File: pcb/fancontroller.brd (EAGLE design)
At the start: 42.5 x 63.3 mm, 109 parts, among them CN1 USB-MICROB-2TABS, Q1 AO3401, Q10 AO3401, Q11 AO3402, Q12 AO3402, Q13 AO3402, Q14 AO3402, Q15 AO3402, Q16 AO3402, Q17 AO3402, Q18 AO3402, Q2 AO3401, Q3 AO3401, Q4 AO3401, Q5 AO3401, Q6 AO3401, Q7 AO3401, Q8 AO3401, Q9 8M, U1 RT9193, U2 STM32F103-48LQFP

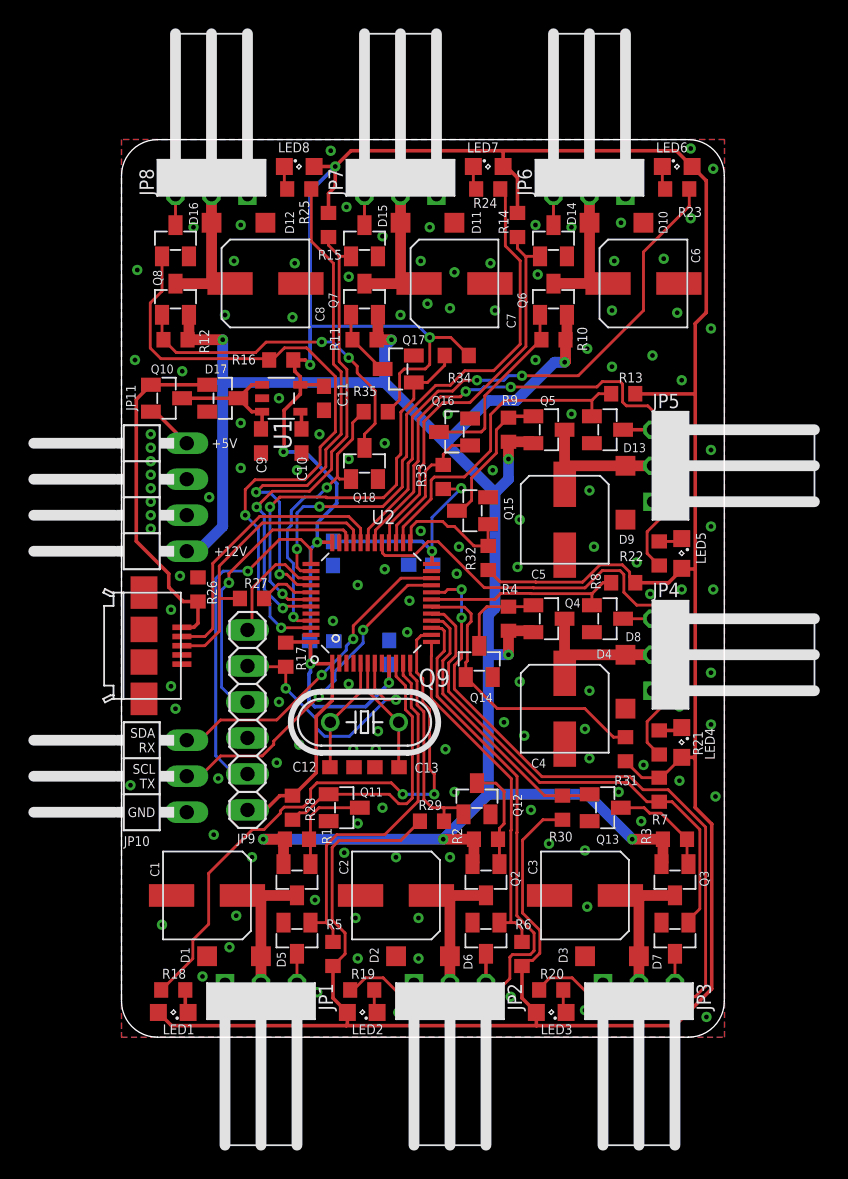
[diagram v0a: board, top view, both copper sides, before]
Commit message: pcb: Move misc designators for better readability
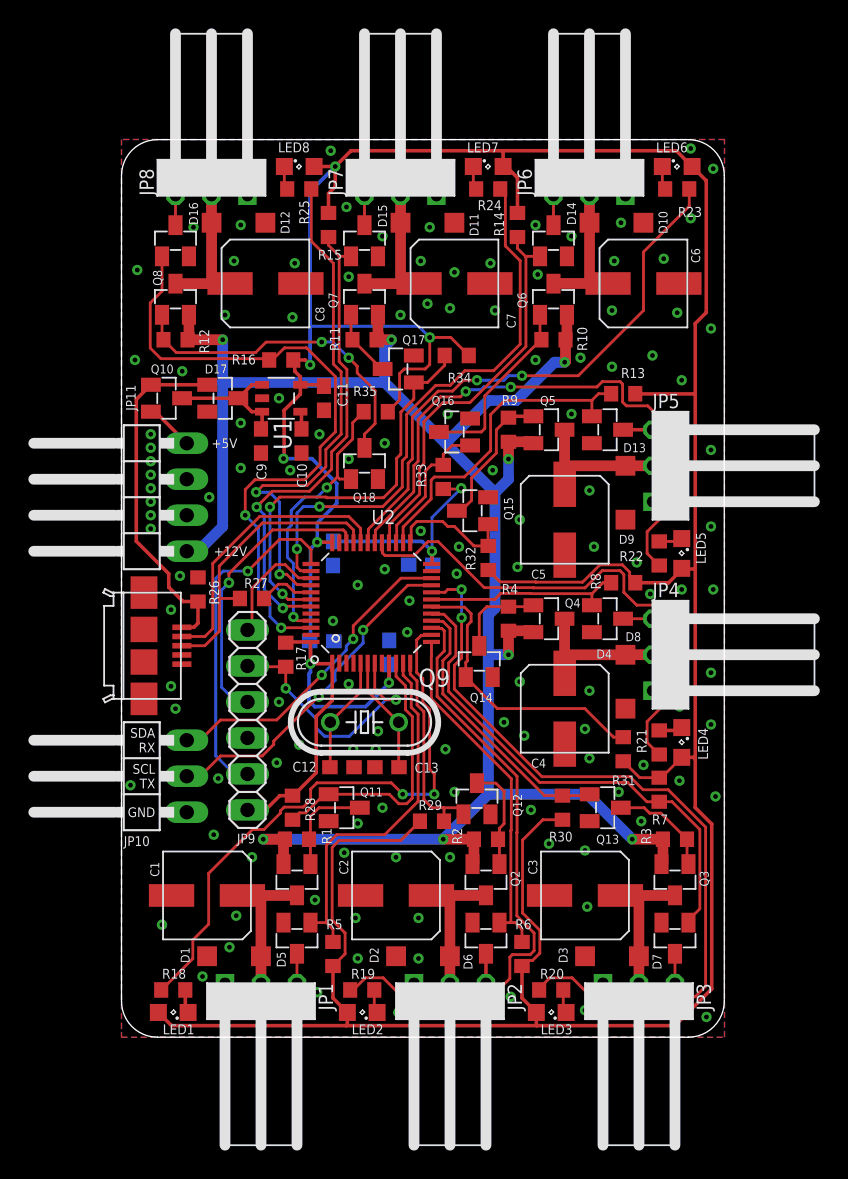
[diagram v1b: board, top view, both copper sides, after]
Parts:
- moved R31 0.16 mm to (35.4, 21.9)
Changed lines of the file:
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@@
 <layer number="46" name="Milling" color="3" fill="1" visible="no" active="yes"/>
 <layer number="47" name="Measures" color="7" fill="1" visible="no" active="yes"/>
-<layer number="48" name="Document" color="7" fill="1" visible="no" active="yes"/>
-<layer number="49" name="Reference" color="7" fill="1" visible="no" active="yes"/>
+<layer number="48" name="Document" color="7" fill="1" visible="yes" active="yes"/>
+<layer number="49" name="Reference" color="7" fill="1" visible="yes" active="yes"/>
 <layer number="50" name="dxf" color="7" fill="1" visible="no" active="no"/>
 <layer number="51" name="tDocu" color="7" fill="1" visible="yes" active="yes"/>
@@
 </element>
 <element name="LED4" library="led" package="SML0805" value="" x="39.52875" y="22.38375" smashed="yes" rot="R270">
-<attribute name="NAME" x="41.16375" y="23.4075" size="0.7" layer="25" rot="R270"/>
+<attribute name="NAME" x="40.6875" y="23.4075" size="0.7" layer="25" rot="R270"/>
 <attribute name="VALUE" x="37.52875" y="23.88375" size="1.27" layer="27" rot="R270"/>
 </element>
@@
 </element>
 <element name="R21" library="tuetuopay" package="R0603" value="330" x="37.94125" y="22.38375" smashed="yes" rot="R90">
-<attribute name="NAME" x="40.3225" y="23.1775" size="0.7" layer="25" rot="R270"/>
+<attribute name="NAME" x="36.35375" y="23.33625" size="0.7" layer="25" rot="R270"/>
 </element>
 <element name="R22" library="tuetuopay" package="R0603" value="330" x="37.94125" y="35.71875" smashed="yes" rot="R90">
@@
 </element>
 <element name="R24" library="tuetuopay" package="R0603" value="330" x="25.87625" y="61.43625" smashed="yes" rot="R180">
-<attribute name="NAME" x="26.51125" y="60.80125" size="0.7" layer="25" rot="R180"/>
+<attribute name="NAME" x="26.82875" y="60.6425" size="0.7" layer="25" rot="R180"/>
 </element>
 <element name="R25" library="tuetuopay" package="R0603" value="330" x="12.54125" y="61.43625" smashed="yes" rot="R180">
@@
 </element>
 <element name="R13" library="tuetuopay" package="R0603" value="10k" x="35.40125" y="46.99" smashed="yes">
-<attribute name="NAME" x="35.08375" y="47.78375" size="0.7" layer="25"/>
+<attribute name="NAME" x="35.2425" y="48.10125" size="0.7" layer="25"/>
 </element>
 <element name="R10" library="tuetuopay" package="R0603" value="100k" x="30.48" y="50.8" smashed="yes">
@@
 </element>
 <element name="R14" library="tuetuopay" package="R0603" value="10k" x="27.94" y="58.89625" smashed="yes" rot="R90">
-<attribute name="NAME" x="27.305" y="58.26125" size="0.7" layer="25" rot="R90"/>
+<attribute name="NAME" x="26.9875" y="58.1025" size="0.7" layer="25" rot="R90"/>
 </element>
 <element name="R11" library="tuetuopay" package="R0603" value="100k" x="17.145" y="50.8" smashed="yes">
@@
 </element>
 <element name="C9" library="tuetuopay" package="0603" value="1u" x="9.8425" y="43.65625" smashed="yes" rot="R270">
-<attribute name="NAME" x="9.525" y="42.545" size="0.7" layer="25" rot="R270"/>
+<attribute name="NAME" x="9.525" y="42.06875" size="0.7" layer="25" rot="R270"/>
 </element>
 <element name="C11" library="tuetuopay" package="0603" value="1u" x="14.2875" y="46.6725" smashed="yes" rot="R270">
@@
 </element>
 <element name="C10" library="tuetuopay" package="0603" value="22n" x="12.7" y="43.65625" smashed="yes" rot="R270">
-<attribute name="NAME" x="12.3825" y="42.545" size="0.7" layer="25" rot="R270"/>
+<attribute name="NAME" x="12.3825" y="42.06875" size="0.7" layer="25" rot="R270"/>
 </element>
 <element name="D17" library="tuetuopay" package="SOT23-3" value="BAS16" x="7.14375" y="46.6725" smashed="yes" rot="R270">
@@
 </element>
 <element name="R26" library="tuetuopay" package="R0603" value="" x="5.3975" y="33.17875" smashed="yes" rot="R270">
-<attribute name="NAME" x="6.0325" y="33.81375" size="0.7" layer="25" rot="R270"/>
+<attribute name="NAME" x="6.19125" y="33.81375" size="0.7" layer="25" rot="R270"/>
 <attribute name="VALUE" x="3.4925" y="33.81375" size="1.27" layer="27" rot="R270"/>
 </element>
@@
 <attribute name="NAME" x="30.1625" y="15.39875" size="0.6858" layer="25"/>
 </element>
-<element name="R31" library="tuetuopay" package="R0603" value="10k" x="35.56" y="21.9075" smashed="yes" rot="R270">
-<attribute name="NAME" x="34.76625" y="19.3675" size="0.6858" layer="25"/>
+<element name="R31" library="tuetuopay" package="R0603" value="10k" x="35.40125" y="21.9075" smashed="yes" rot="R270">
+<attribute name="NAME" x="34.6075" y="19.3675" size="0.6858" layer="25"/>
 </element>
 <element name="R32" library="tuetuopay" package="R0603" value="10k" x="25.87625" y="35.40125" smashed="yes" rot="R270">
@@
 </element>
 <element name="D11" library="tuetuopay" package="SOD123" value="MBR0540T1" x="21.59" y="59.055" smashed="yes">
-<attribute name="NAME" x="25.3525" y="58.2725" size="0.635" layer="25" rot="R90"/>
+<attribute name="NAME" x="25.19375" y="58.11375" size="0.635" layer="25" rot="R90"/>
 </element>
 <element name="D12" library="tuetuopay" package="SOD123" value="MBR0540T1" x="8.255" y="59.055" smashed="yes">
-<attribute name="NAME" x="12.17625" y="58.2725" size="0.635" layer="25" rot="R90"/>
+<attribute name="NAME" x="11.85875" y="58.2725" size="0.635" layer="25" rot="R90"/>
 </element>
 </elements>
@@
 <via x="33.02" y="62.5475" extent="1-16" drill="0.3302"/>
 <via x="29.21" y="58.89625" extent="1-16" drill="0.3302"/>
-<via x="31.75" y="58.7375" extent="1-16" drill="0.3302"/>
+<via x="31.75" y="58.1025" extent="1-16" drill="0.3302"/>
 <via x="26.035" y="56.1975" extent="1-16" drill="0.3302"/>
 <via x="23.495" y="55.5625" extent="1-16" drill="0.3302"/>
@@
 <via x="29.21" y="49.37125" extent="1-16" drill="0.3302"/>
 <via x="34.6075" y="52.86375" extent="1-16" drill="0.3302"/>
-<via x="32.86125" y="50.165" extent="1-16" drill="0.3302"/>
+<via x="32.385" y="49.53" extent="1-16" drill="0.3302"/>
 <via x="40.16375" y="64.29375" extent="1-16" drill="0.3302"/>
 <via x="41.75125" y="62.865" extent="1-16" drill="0.3302"/>
@@
 <via x="36.67125" y="16.8275" extent="1-16" drill="0.3302"/>
 <via x="23.8125" y="36.195" extent="1-16" drill="0.3302"/>
-<via x="12.3825" y="41.5925" extent="1-16" drill="0.3302"/>
+<via x="11.90625" y="41.5925" extent="1-16" drill="0.3302"/>
 <contactref element="Q11" pad="2"/>
 <contactref element="Q12" pad="2"/>
@@
 <wire x1="12.62125" y1="47.6225" x2="12.62125" y2="46.964475" width="0.254" layer="1"/>
 <wire x1="12.62125" y1="46.964475" x2="11.47355" y2="45.816775" width="0.254" layer="1"/>
-<wire x1="11.47355" y1="42.93146875" x2="11.43" y2="42.88791875" width="0.254" layer="1"/>
-<wire x1="11.47355" y1="45.816775" x2="11.47355" y2="42.93146875" width="0.254" layer="1"/>
-<via x="11.43" y="42.88791875" extent="1-16" drill="0.3302"/>
+<wire x1="11.47355" y1="42.45521875" x2="11.43" y2="42.41166875" width="0.254" layer="1"/>
+<wire x1="11.47355" y1="45.816775" x2="11.47355" y2="42.45521875" width="0.254" layer="1"/>
+<via x="11.43" y="42.41166875" extent="1-16" drill="0.3302"/>
 <wire x1="13.95095" y1="36.53155" x2="13.81125" y2="36.5125" width="0.254" layer="16"/>
 <wire x1="13.81125" y1="36.5125" x2="13.335" y2="36.03625" width="0.254" layer="16"/>
@@
 <wire x1="13.81125" y1="36.5125" x2="13.81125" y2="37.88051875" width="0.254" layer="16"/>
 <wire x1="13.81125" y1="37.88051875" x2="15.1864125" y2="39.25568125" width="0.254" layer="16"/>
-<wire x1="15.1864125" y1="40.66263125" x2="12.961125" y2="42.88791875" width="0.254" layer="16"/>
-<wire x1="12.961125" y1="42.88791875" x2="11.43" y2="42.88791875" width="0.254" layer="16"/>
+<wire x1="15.1864125" y1="40.66263125" x2="13.437375" y2="42.41166875" width="0.254" layer="16"/>
+<wire x1="13.437375" y1="42.41166875" x2="11.43" y2="42.41166875" width="0.254" layer="16"/>
 <wire x1="15.1864125" y1="39.25568125" x2="15.1864125" y2="40.66263125" width="0.254" layer="16"/>
 <wire x1="18.78875" y1="45.72" x2="19.62145" y2="46.5527" width="0.2032" layer="1"/>
@@
 <wire x1="13.7414" y1="20.25015" x2="12.12125" y2="18.63" width="0.254" layer="1"/>
 <wire x1="13.7414" y1="24.222825" x2="13.7414" y2="20.25015" width="0.254" layer="1"/>
-<wire x1="35.56" y1="21.0575" x2="36.7175" y2="19.9" width="0.2032" layer="1"/>
-<wire x1="36.7175" y1="19.9" x2="37.94125" y2="19.9" width="0.2032" layer="1"/>
+<wire x1="35.40125" y1="21.0575" x2="36.55875" y2="19.9" width="0.2032" layer="1"/>
+<wire x1="36.55875" y1="19.9" x2="37.94125" y2="19.9" width="0.2032" layer="1"/>
 </signal>
 <signal name="SWDIO">
@@
 <wire x1="26.51375" y1="24.77625" x2="32.69125" y2="24.77625" width="0.2032" layer="1"/>
 <wire x1="32.69125" y1="24.77625" x2="34.71" y2="22.7575" width="0.2032" layer="1"/>
-<wire x1="34.71" y1="22.7575" x2="35.56" y2="22.7575" width="0.2032" layer="1"/>
+<wire x1="34.71" y1="22.7575" x2="35.40125" y2="22.7575" width="0.2032" layer="1"/>
 </signal>
 <signal name="TAC3">
